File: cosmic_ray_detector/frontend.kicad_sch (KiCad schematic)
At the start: 15 parts, among them U1 TL072

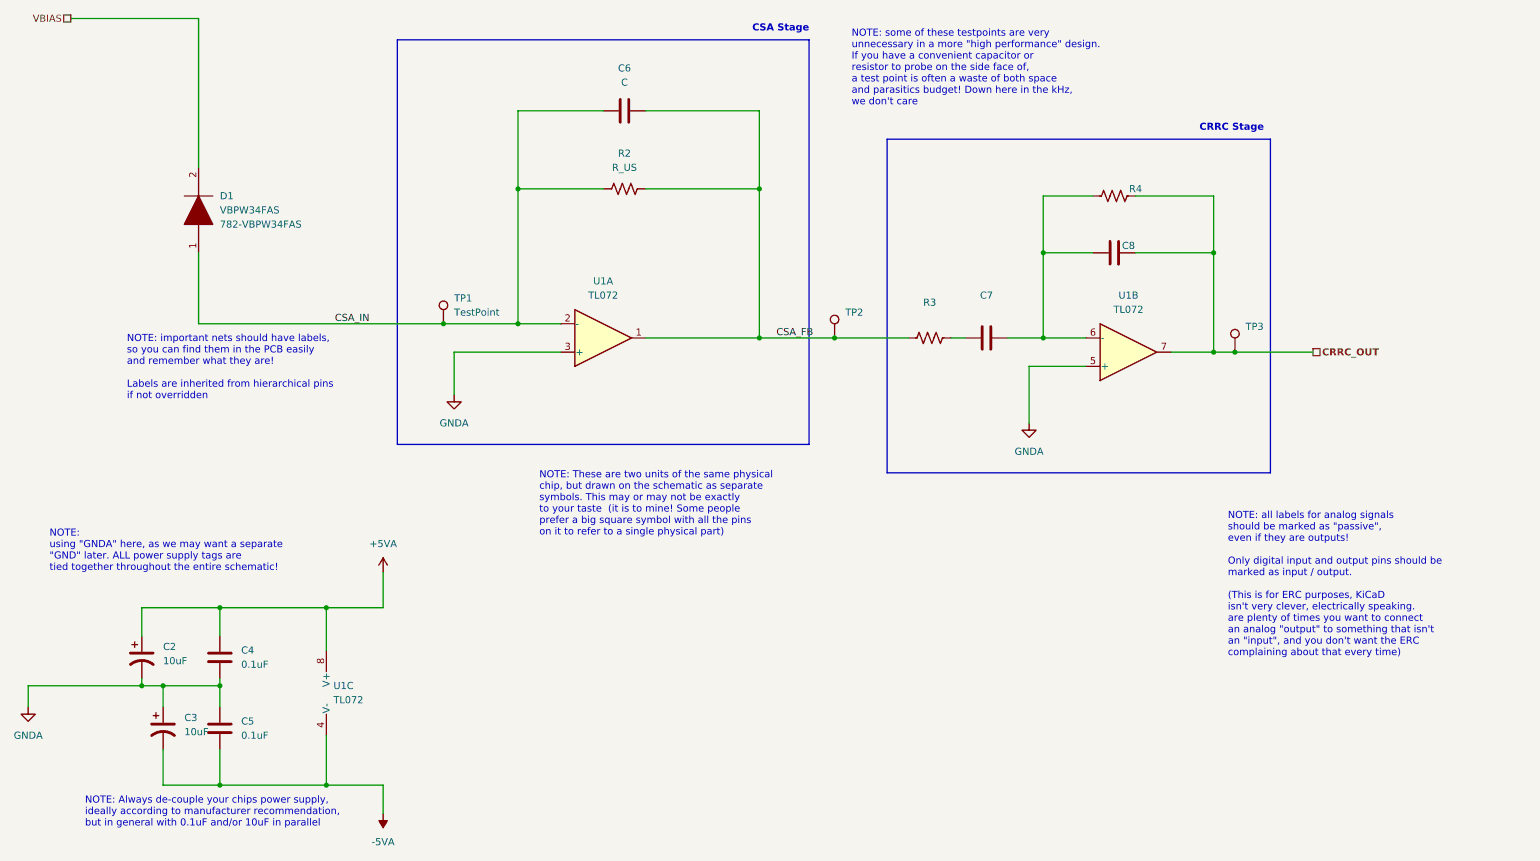
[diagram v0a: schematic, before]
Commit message: changed a couple more caps
all components reasonably grouped, almost placed
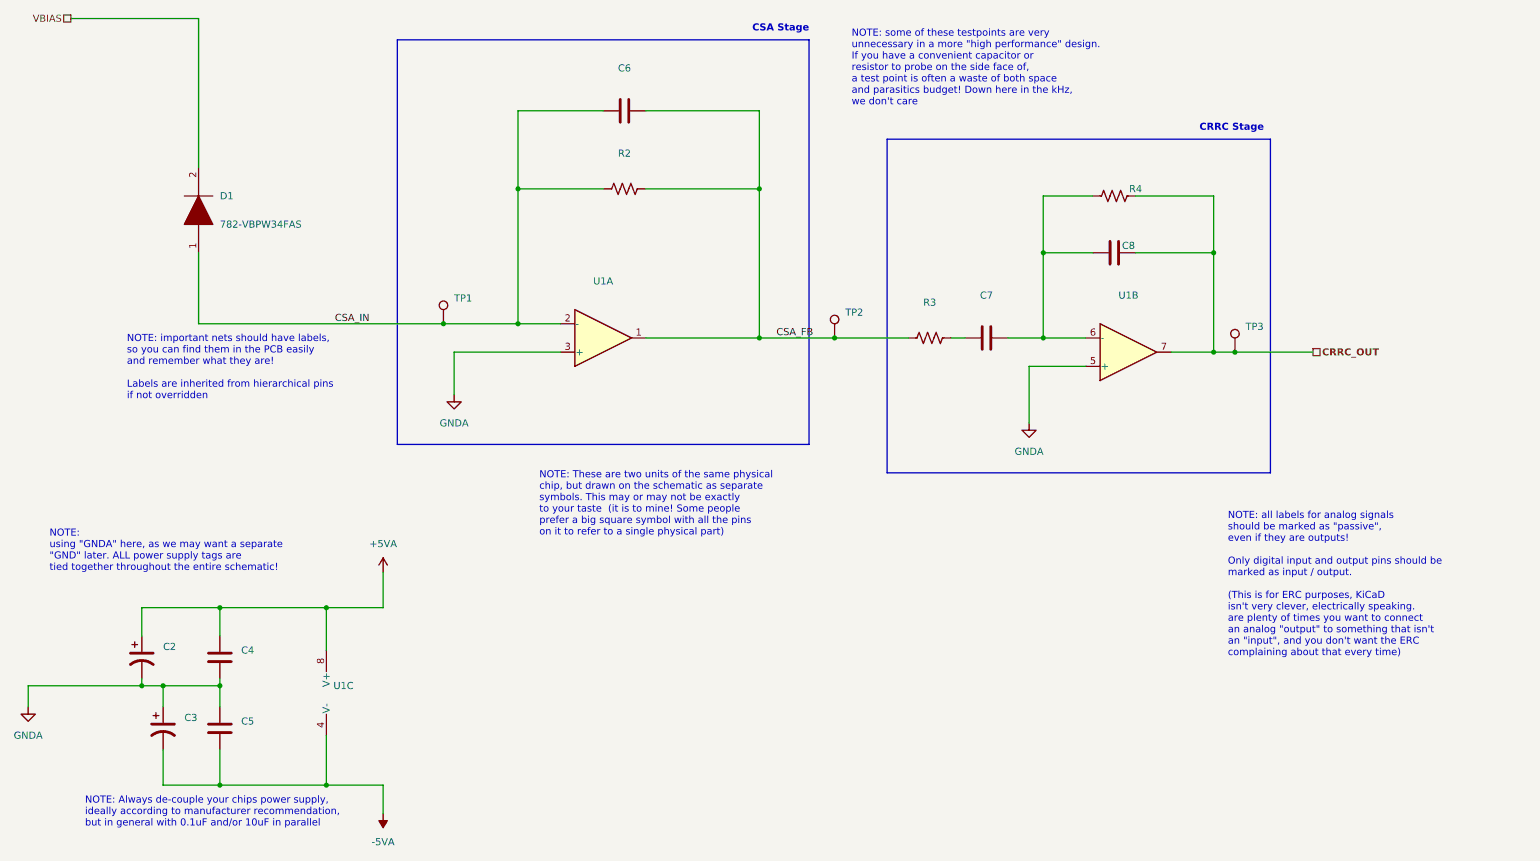
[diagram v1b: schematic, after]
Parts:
- C2, C3: value 10uF -> (none); footprint cosmic_ray_detector_lib:MAL215375109E3 -> (none); Farnell 1187014 -> 1432339; MPN MAL215375109E3 -> TAJA106K016RNJ; Manufacturer_Name Vishay -> Kyocera AVX
- C4, C5: value 0.1uF -> (none); footprint Capacitor_SMD:C_0402_1005Metric -> (none)
- C6: value C -> (none); footprint Capacitor_SMD:C_0402_1005Metric -> (none)
- C7, C8: value ~ -> (none); footprint Capacitor_SMD:C_0402_1005Metric -> (none)
- D1: value VBPW34FAS -> (none); footprint cosmic_ray_detector_lib:VBPW34FAS -> (none)
- R2: value R_US -> (none); footprint Resistor_SMD:R_0402_1005Metric -> (none)
- R3, R4: value ~ -> (none); footprint Resistor_SMD:R_0402_1005Metric -> (none)
- TP1: value TestPoint -> (none); footprint cosmic_ray_detector_lib:harwin_tp_SMD -> (none)
- TP2, TP3: value ~ -> (none); footprint cosmic_ray_detector_lib:harwin_tp_SMD -> (none)
- U1: value TL072 -> (none); footprint Package_SO:SO-8_3.9x4.9mm_P1.27mm -> (none)
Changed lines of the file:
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@@
     (in_bom yes) (on_board yes) (fields_autoplaced)
     (property "Reference" "U1" (id 0) (at 219.71 97.79 0))
-    (property "Value" "TL072" (id 1) (at 219.71 100.33 0))
-    (property "Footprint" "Package_SO:SO-8_3.9x4.9mm_P1.27mm" (id 2) (at 219.71 107.95 0)
+    (property "Value" "" (id 1) (at 219.71 100.33 0))
+    (property "Footprint" "" (id 2) (at 219.71 107.95 0)
       (effects (font (size 1.27 1.27)) hide)
     )
@@
     (in_bom yes) (on_board yes)
     (property "Reference" "R4" (id 0) (at 220.98 78.74 90))
-    (property "Value" "~" (id 1) (at 217.17 76.2 90))
-    (property "Footprint" "Resistor_SMD:R_0402_1005Metric" (id 2) (at 217.424 78.994 90)
+    (property "Value" "" (id 1) (at 217.17 76.2 90))
+    (property "Footprint" "" (id 2) (at 217.424 78.994 90)
       (effects (font (size 1.27 1.27)) hide)
     )
@@
     (in_bom yes) (on_board yes) (fields_autoplaced)
     (property "Reference" "C7" (id 0) (at 194.31 97.79 90))
-    (property "Value" "~" (id 1) (at 194.31 100.33 90))
-    (property "Footprint" "Capacitor_SMD:C_0402_1005Metric" (id 2) (at 198.12 104.4448 0)
+    (property "Value" "" (id 1) (at 194.31 100.33 90))
+    (property "Footprint" "" (id 2) (at 198.12 104.4448 0)
       (effects (font (size 1.27 1.27)) hide)
     )
@@
     (in_bom yes) (on_board yes) (fields_autoplaced)
     (property "Reference" "R2" (id 0) (at 129.54 72.39 90))
-    (property "Value" "R_US" (id 1) (at 129.54 74.93 90))
-    (property "Footprint" "Resistor_SMD:R_0402_1005Metric" (id 2) (at 129.794 77.724 90)
+    (property "Value" "" (id 1) (at 129.54 74.93 90))
+    (property "Footprint" "" (id 2) (at 129.794 77.724 90)
       (effects (font (size 1.27 1.27)) hide)
     )
@@
       (effects (font (size 1.27 1.27)) (justify left))
     )
-    (property "Value" "VBPW34FAS" (id 1) (at 57.15 82.5499 90)
-      (effects (font (size 1.27 1.27)) (justify left))
-    )
-    (property "Footprint" "cosmic_ray_detector_lib:VBPW34FAS" (id 2) (at 53.34 86.36 0)
+    (property "Value" "" (id 1) (at 57.15 82.5499 90)
+      (effects (font (size 1.27 1.27)) (justify left))
+    )
+    (property "Footprint" "" (id 2) (at 53.34 86.36 0)
       (effects (font (size 1.27 1.27)) (justify left) hide)
     )
@@
       (effects (font (size 1.27 1.27)) (justify left))
     )
-    (property "Value" "0.1uF" (id 1) (at 60.96 163.8299 0)
-      (effects (font (size 1.27 1.27)) (justify left))
-    )
-    (property "Footprint" "Capacitor_SMD:C_0402_1005Metric" (id 2) (at 58.1152 166.37 0)
+    (property "Value" "" (id 1) (at 60.96 163.8299 0)
+      (effects (font (size 1.27 1.27)) (justify left))
+    )
+    (property "Footprint" "" (id 2) (at 58.1152 166.37 0)
       (effects (font (size 1.27 1.27)) hide)
     )
@@
       (effects (font (size 1.27 1.27)) (justify left))
     )
-    (property "Value" "10uF" (id 1) (at 50.8 175.8949 0)
-      (effects (font (size 1.27 1.27)) (justify left))
-    )
-    (property "Footprint" "cosmic_ray_detector_lib:MAL215375109E3" (id 2) (at 46.99 175.26 0)
+    (property "Value" "" (id 1) (at 50.8 175.8949 0)
+      (effects (font (size 1.27 1.27)) (justify left))
+    )
+    (property "Footprint" "" (id 2) (at 46.99 175.26 0)
       (effects (font (size 1.27 1.27)) hide)
     )
@@
       (effects (font (size 1.27 1.27)) hide)
     )
-    (property "Farnell" "1187014 " (id 4) (at 46.99 175.26 0)
-      (effects (font (size 1.27 1.27)) hide)
-    )
-    (property "MPN" "MAL215375109E3" (id 5) (at 46.99 175.26 0)
-      (effects (font (size 1.27 1.27)) hide)
-    )
-    (property "Manufacturer_Name" "Vishay" (id 6) (at 46.99 175.26 0)
+    (property "Farnell" "1432339" (id 4) (at 46.99 175.26 0)
+      (effects (font (size 1.27 1.27)) hide)
+    )
+    (property "MPN" "TAJA106K016RNJ" (id 5) (at 46.99 175.26 0)
+      (effects (font (size 1.27 1.27)) hide)
+    )
+    (property "Manufacturer_Name" "Kyocera AVX" (id 6) (at 46.99 175.26 0)
       (effects (font (size 1.27 1.27)) hide)
     )
@@
     (in_bom yes) (on_board yes) (fields_autoplaced)
     (property "Reference" "R3" (id 0) (at 184.15 99.06 90))
-    (property "Value" "~" (id 1) (at 184.15 101.6 90))
-    (property "Footprint" "Resistor_SMD:R_0402_1005Metric" (id 2) (at 184.404 104.394 90)
+    (property "Value" "" (id 1) (at 184.15 101.6 90))
+    (property "Footprint" "" (id 2) (at 184.404 104.394 90)
       (effects (font (size 1.27 1.27)) hide)
     )
@@
     (in_bom yes) (on_board yes)
     (property "Reference" "C8" (id 0) (at 219.71 88.9 90))
-    (property "Value" "~" (id 1) (at 217.17 85.09 90))
-    (property "Footprint" "Capacitor_SMD:C_0402_1005Metric" (id 2) (at 220.98 89.2048 0)
+    (property "Value" "" (id 1) (at 217.17 85.09 90))
+    (property "Footprint" "" (id 2) (at 220.98 89.2048 0)
       (effects (font (size 1.27 1.27)) hide)
     )
@@
       (effects (font (size 1.27 1.27)) (justify left))
     )
-    (property "Value" "10uF" (id 1) (at 46.99 163.1949 0)
-      (effects (font (size 1.27 1.27)) (justify left))
-    )
-    (property "Footprint" "cosmic_ray_detector_lib:MAL215375109E3" (id 2) (at 43.18 162.56 0)
+    (property "Value" "" (id 1) (at 46.99 163.1949 0)
+      (effects (font (size 1.27 1.27)) (justify left))
+    )
+    (property "Footprint" "" (id 2) (at 43.18 162.56 0)
       (effects (font (size 1.27 1.27)) hide)
     )
@@
       (effects (font (size 1.27 1.27)) hide)
     )
-    (property "Farnell" "1187014 " (id 4) (at 43.18 162.56 0)
-      (effects (font (size 1.27 1.27)) hide)
-    )
-    (property "MPN" "MAL215375109E3" (id 5) (at 43.18 162.56 0)
-      (effects (font (size 1.27 1.27)) hide)
-    )
-    (property "Manufacturer_Name" "Vishay" (id 6) (at 43.18 162.56 0)
+    (property "Farnell" "1432339" (id 4) (at 43.18 162.56 0)
+      (effects (font (size 1.27 1.27)) hide)
+    )
+    (property "MPN" "TAJA106K016RNJ" (id 5) (at 43.18 162.56 0)
+      (effects (font (size 1.27 1.27)) hide)
+    )
+    (property "Manufacturer_Name" "Kyocera AVX" (id 6) (at 43.18 162.56 0)
       (effects (font (size 1.27 1.27)) hide)
     )
@@
     (in_bom yes) (on_board yes) (fields_autoplaced)
     (property "Reference" "C6" (id 0) (at 129.54 57.15 90))
-    (property "Value" "C" (id 1) (at 129.54 59.69 90))
-    (property "Footprint" "Capacitor_SMD:C_0402_1005Metric" (id 2) (at 133.35 63.8048 0)
+    (property "Value" "" (id 1) (at 129.54 59.69 90))
+    (property "Footprint" "" (id 2) (at 133.35 63.8048 0)
       (effects (font (size 1.27 1.27)) hide)
     )
@@
       (effects (font (size 1.27 1.27)) (justify left))
     )
-    (property "Value" "TestPoint" (id 1) (at 99.06 100.8379 0)
-      (effects (font (size 1.27 1.27)) (justify left))
-    )
-    (property "Footprint" "cosmic_ray_detector_lib:harwin_tp_SMD" (id 2) (at 102.235 102.87 0)
+    (property "Value" "" (id 1) (at 99.06 100.8379 0)
+      (effects (font (size 1.27 1.27)) (justify left))
+    )
+    (property "Footprint" "" (id 2) (at 102.235 102.87 0)
       (effects (font (size 1.27 1.27)) hide)
     )
@@
       (effects (font (size 1.27 1.27)) (justify left))
     )
-    (property "Value" "0.1uF" (id 1) (at 60.96 176.5299 0)
-      (effects (font (size 1.27 1.27)) (justify left))
-    )
-    (property "Footprint" "Capacitor_SMD:C_0402_1005Metric" (id 2) (at 58.1152 179.07 0)
+    (property "Value" "" (id 1) (at 60.96 176.5299 0)
+      (effects (font (size 1.27 1.27)) (justify left))
+    )
+    (property "Footprint" "" (id 2) (at 58.1152 179.07 0)
       (effects (font (size 1.27 1.27)) hide)
     )
@@
       (effects (font (size 1.27 1.27)) (justify left))
     )
-    (property "Value" "~" (id 1) (at 169.037 103.3779 0)
-      (effects (font (size 1.27 1.27)) (justify left))
-    )
-    (property "Footprint" "cosmic_ray_detector_lib:harwin_tp_SMD" (id 2) (at 172.212 105.41 0)
+    (property "Value" "" (id 1) (at 169.037 103.3779 0)
+      (effects (font (size 1.27 1.27)) (justify left))
+    )
+    (property "Footprint" "" (id 2) (at 172.212 105.41 0)
       (effects (font (size 1.27 1.27)) hide)
     )
@@
     (in_bom yes) (on_board yes) (fields_autoplaced)
     (property "Reference" "U1" (id 0) (at 125.73 95.25 0))
-    (property "Value" "TL072" (id 1) (at 125.73 97.79 0))
-    (property "Footprint" "Package_SO:SO-8_3.9x4.9mm_P1.27mm" (id 2) (at 125.73 105.41 0)
+    (property "Value" "" (id 1) (at 125.73 97.79 0))
+    (property "Footprint" "" (id 2) (at 125.73 105.41 0)
       (effects (font (size 1.27 1.27)) hide)
     )
@@
       (effects (font (size 1.27 1.27)) (justify left))
     )
-    (property "Value" "TL072" (id 1) (at 77.47 170.1799 0)
-      (effects (font (size 1.27 1.27)) (justify left))
-    )
-    (property "Footprint" "Package_SO:SO-8_3.9x4.9mm_P1.27mm" (id 2) (at 78.74 168.91 0)
+    (property "Value" "" (id 1) (at 77.47 170.1799 0)
+      (effects (font (size 1.27 1.27)) (justify left))
+    )
+    (property "Footprint" "" (id 2) (at 78.74 168.91 0)
       (effects (font (size 1.27 1.27)) hide)
     )
@@
       (effects (font (size 1.27 1.27)) (justify left))
     )
-    (property "Value" "~" (id 1) (at 240.665 105.9179 0)
-      (effects (font (size 1.27 1.27)) (justify left))
-    )
-    (property "Footprint" "cosmic_ray_detector_lib:harwin_tp_SMD" (id 2) (at 243.84 107.95 0)
-      (effects (font (size 1.27 1.27)) hide)
-    )
+    (property "Value" "" (id 1) (at 240.665 105.9179 0)
+      (effects (font (size 1.27 1.27)) (justify left))
+    )
+    (property "Footprint" "" (id 2) (at 243.84 107.95 0)
+      (effects (font (size 1.27 1.27)) hide)
+    )

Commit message: update autorouting branch to v8
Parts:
- C2, C3: value (none) -> 10uF; footprint (none) -> Capacitor_Tantalum_SMD:CP_EIA-3216-12_Kemet-S
- C4, C5: value (none) -> 0.1uF; footprint (none) -> Capacitor_SMD:C_0402_1005Metric
- C6: value (none) -> C; footprint (none) -> Capacitor_SMD:C_0402_1005Metric
- C7, C8: value (none) -> ~; footprint (none) -> Capacitor_SMD:C_0402_1005Metric
- D1: value (none) -> VBPW34FAS; footprint (none) -> cosmic_ray_detector_lib:VBPW34FAS
- R2: value (none) -> R_US; footprint (none) -> Resistor_SMD:R_0402_1005Metric
- R3, R4: value (none) -> ~; footprint (none) -> Resistor_SMD:R_0402_1005Metric
- TP1: value (none) -> TestPoint; footprint (none) -> cosmic_ray_detector_lib:harwin_tp_SMD
- TP2, TP3: value (none) -> ~; footprint (none) -> cosmic_ray_detector_lib:harwin_tp_SMD
- U1: value (none) -> TL072; footprint (none) -> Package_SO:SO-8_3.9x4.9mm_P1.27mm
